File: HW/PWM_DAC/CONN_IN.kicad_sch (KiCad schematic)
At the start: 2 parts, among them J401 Conn_01x08, J402 Conn_01x07

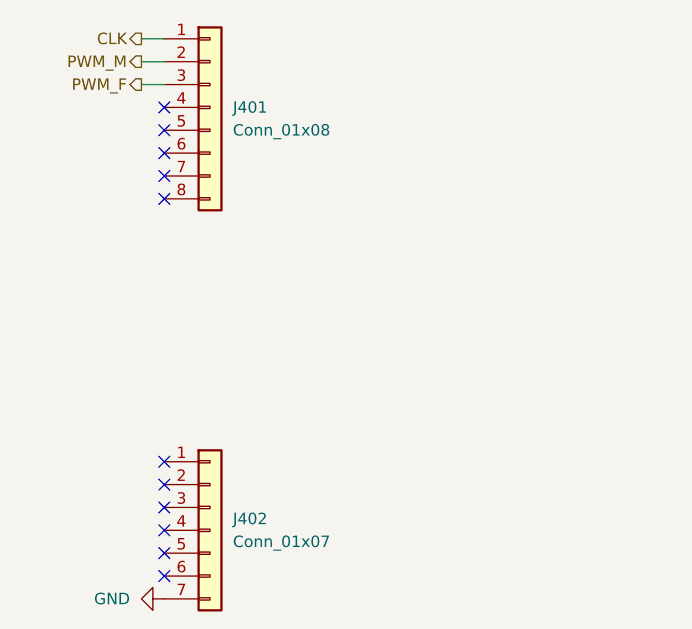
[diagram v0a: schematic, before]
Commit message: Schematic done
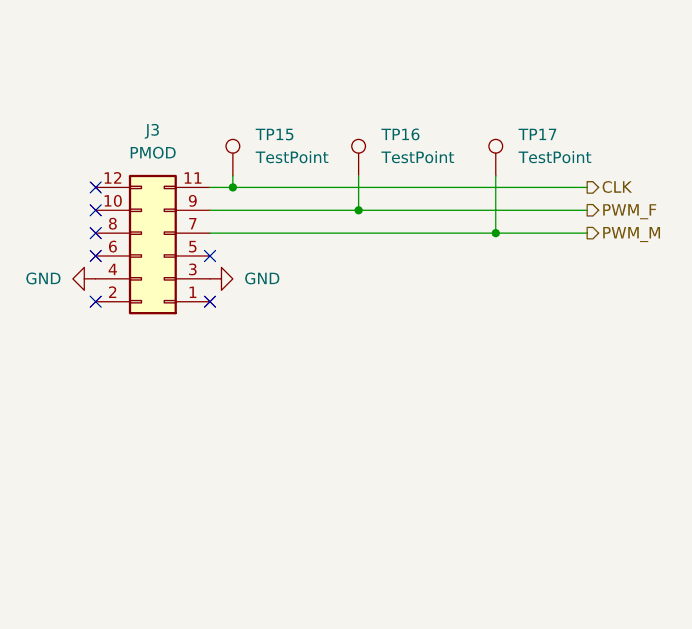
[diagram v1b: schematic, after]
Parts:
- removed J401: Conn_01x08, Connector_PinHeader_2.54mm:PinHeader_1x08_P2.54mm_Vertical_SMD_Pin1Right, symbol Connector_Generic:Conn_01x08
- removed J402: Conn_01x07, Connector_PinHeader_2.54mm:PinHeader_1x07_P2.54mm_Vertical_SMD_Pin1Right, symbol Connector_Generic:Conn_01x07
- added J3: PMOD, Connector_PinHeader_2.54mm:PinHeader_2x06_P2.54mm_Horizontal, symbol Connector_Generic:Conn_02x06_Odd_Even
- added TP15, TP16, TP17: TestPoint, TestPoint:TestPoint_Pad_D1.5mm, symbol Connector:TestPoint
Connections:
- net CLK: now also J3.11 (Pin_11), TP15.1
- net GND: now also J3.3 (Pin_3), J3.4 (Pin_4)
- net PWM_F: now also J3.9 (Pin_9), TP16.1
- net PWM_M: now also J3.7 (Pin_7), TP17.1
- no-connect marks 11 -> 7

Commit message: Layout done
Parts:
- renumbered TP15 to TP24, TP16 to TP25, TP17 to TP26
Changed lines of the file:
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@@
+		)
+	)
+	(rule_area
+		(exclude_from_sim no)
+		(in_bom yes)
+		(on_board yes)
+		(dnp no)
+		(polyline
+			(pts
+				(xy 13.97 16.51) (xy 406.4 16.51) (xy 406.4 251.46) (xy 298.45 251.46) (xy 298.45 283.21) (xy 13.97 283.21)
+			)
+			(stroke
+				(width 0)
+				(type dash)
+			)
+			(fill
+				(type none)
+			)
+		)
+	)
+	(netclass_flag ""
+		(length 2.54)
+		(shape round)
+		(at 13.97 16.51 0)
+		(fields_autoplaced yes)
+		(effects
+			(font
+				(size 1.27 1.27)
+			)
+			(justify left bottom)
+		)
+		(property "Netclass" "GND"
+			(at 14.6685 13.97 0)
+			(show_name no)
+			(do_not_autoplace no)
+			(effects
+				(font
+					(size 1.27 1.27)
+				)
+				(justify left)
+			)
+		)
+		(property "Component Class" ""
+			(at -640.08 -81.28 0)
+			(show_name no)
+			(do_not_autoplace no)
+			(effects
+				(font
+					(size 1.27 1.27)
+					(italic yes)
+				)
+			)
 		)
 	)
@@
 		(dnp no)
 		(fields_autoplaced yes)
-		(property "Reference" "#PWR095"
+		(property "Reference" "#PWR094"
 			(at 195.58 121.92 0)
 			(hide yes)
@@
 			(project "PWM_DAC"
 				(path "/2c9a3dd6-931b-4123-b00f-9baea7dc6b77/733b56bb-668f-4cc4-94fb-a3b617279a5b"
-					(reference "#PWR095")
+					(reference "#PWR094")
 					(unit 1)
 				)
@@
 		(dnp no)
 		(fields_autoplaced yes)
-		(property "Reference" "TP16"
+		(property "Reference" "TP25"
 			(at 233.68 105.9179 0)
 			(show_name no)
@@
 		)
 		(property "KLC_S4.5" ""
+			(at 231.14 110.49 0)
+			(hide yes)
+			(show_name no)
+			(do_not_autoplace no)
+			(effects
+				(font
+					(size 1.27 1.27)
+				)
+			)
+		)
+		(property "Sim.Device" ""
+			(at 231.14 110.49 0)
+			(hide yes)
+			(show_name no)
+			(do_not_autoplace no)
+			(effects
+				(font
+					(size 1.27 1.27)
+				)
+			)
+		)
+		(property "Sim.Pins" ""
 			(at 231.14 110.49 0)
 			(hide yes)
@@
 			(project "PWM_DAC"
 				(path "/2c9a3dd6-931b-4123-b00f-9baea7dc6b77/733b56bb-668f-4cc4-94fb-a3b617279a5b"
-					(reference "TP16")
+					(reference "TP25")
 					(unit 1)
 				)
@@
 			)
 		)
+		(property "Sim.Device" ""
+			(at 209.55 119.38 0)
+			(hide yes)
+			(show_name no)
+			(do_not_autoplace no)
+			(effects
+				(font
+					(size 1.27 1.27)
+				)
+			)
+		)
+		(property "Sim.Pins" ""
+			(at 209.55 119.38 0)
+			(hide yes)
+			(show_name no)
+			(do_not_autoplace no)
+			(effects
+				(font
+					(size 1.27 1.27)
+				)
+			)
+		)
 		(pin "4"
 		)
@@
 		(dnp no)
 		(fields_autoplaced yes)
-		(property "Reference" "#PWR096"
+		(property "Reference" "#PWR095"
 			(at 220.98 121.92 0)
 			(hide yes)
@@
 			(project "PWM_DAC"
 				(path "/2c9a3dd6-931b-4123-b00f-9baea7dc6b77/733b56bb-668f-4cc4-94fb-a3b617279a5b"
-					(reference "#PWR096")
+					(reference "#PWR095")
 					(unit 1)
 				)
@@
 		(dnp no)
 		(fields_autoplaced yes)
-		(property "Reference" "TP17"
+		(property "Reference" "TP26"
 			(at 248.92 105.9179 0)
 			(show_name no)
@@
 		)
 		(property "KLC_S4.5" ""
+			(at 246.38 110.49 0)
+			(hide yes)
+			(show_name no)
+			(do_not_autoplace no)
+			(effects
+				(font
+					(size 1.27 1.27)
+				)
+			)
+		)
+		(property "Sim.Device" ""
+			(at 246.38 110.49 0)
+			(hide yes)
+			(show_name no)
+			(do_not_autoplace no)
+			(effects
+				(font
+					(size 1.27 1.27)
+				)
+			)
+		)
+		(property "Sim.Pins" ""
 			(at 246.38 110.49 0)
 			(hide yes)
@@
 			(project "PWM_DAC"
 				(path "/2c9a3dd6-931b-4123-b00f-9baea7dc6b77/733b56bb-668f-4cc4-94fb-a3b617279a5b"
-					(reference "TP17")
+					(reference "TP26")
 					(unit 1)
 				)
@@
 		(dnp no)
 		(fields_autoplaced yes)
-		(property "Reference" "TP15"
+		(property "Reference" "TP24"
 			(at 219.71 105.9179 0)
 			(show_name no)
@@
 		)
 		(property "KLC_S4.5" ""
+			(at 217.17 110.49 0)
+			(hide yes)
+			(show_name no)
+			(do_not_autoplace no)
+			(effects
+				(font
+					(size 1.27 1.27)
+				)
+			)
+		)
+		(property "Sim.Device" ""
+			(at 217.17 110.49 0)
+			(hide yes)
+			(show_name no)
+			(do_not_autoplace no)
+			(effects
+				(font
+					(size 1.27 1.27)
+				)
+			)
+		)
+		(property "Sim.Pins" ""
 			(at 217.17 110.49 0)
 			(hide yes)
@@
 			(project "PWM_DAC"
 				(path "/2c9a3dd6-931b-4123-b00f-9baea7dc6b77/733b56bb-668f-4cc4-94fb-a3b617279a5b"
-					(reference "TP15")
+					(reference "TP24")
 					(unit 1)
 				)
